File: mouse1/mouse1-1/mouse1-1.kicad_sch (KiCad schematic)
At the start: 30 parts

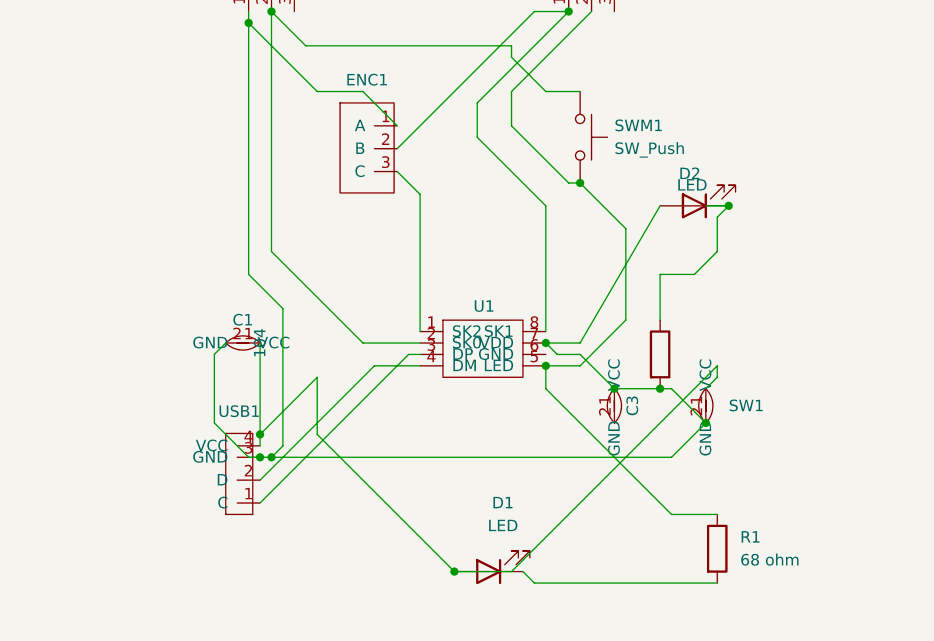
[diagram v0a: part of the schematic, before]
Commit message: Finished PCB - added full labels and all components, even if not actually soldered
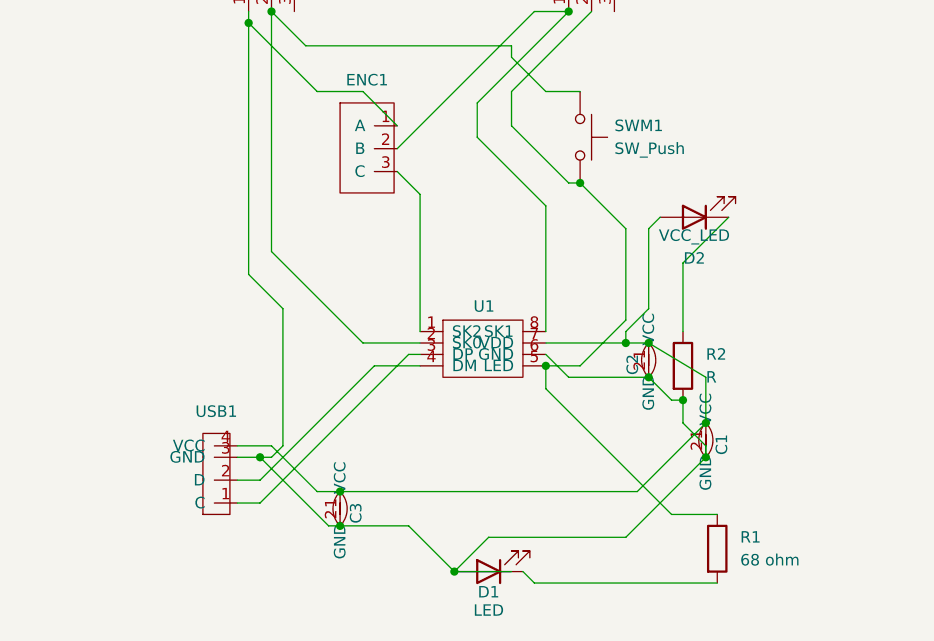
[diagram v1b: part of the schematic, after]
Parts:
- removed D2: LED, LED_THT:LED_D3.0mm_Horizontal_O1.27mm_Z2.0mm, symbol Device:LED
- removed SW1: (no value), IllinoisCapacitor_r3mm_h8mm:IllinoisCapacitor_r3mm_h8mm, symbol SmallCapacitor:SC
- added C2: (no value), SmallCapacitor:SmallCapacitor, symbol SmallCapacitor:SC
- added D2: VCC_LED, LED_THT:LED_D3.0mm_Horizontal_O1.27mm_Z2.0mm, symbol VCC_LED:VCC_LED
- C1: value 104 -> (none); footprint IllinoisCapacitor_r3mm_h8mm:IllinoisCapacitor_r3mm_h8mm -> SmallCapacitor:SmallCapacitor
- C3: footprint IllinoisCapacitor_r3mm_h8mm:IllinoisCapacitor_r3mm_h8mm -> SmallCapacitor:SmallCapacitor; now left out of the parts list
- R2: value 68 ohm -> R; footprint Resistor_THT:R_Axial_DIN0204_L3.6mm_D1.6mm_P5.08mm_Horizontal -> Resistor_THT:R_Axial_DIN0204_L3.6mm_D1.6mm_P5.08mm_Vertical; now left out of the parts list
- SWM1: footprint SW_PUSH_6mm_h7.3mm-2pin:SW_PUSH_6mm_h7.3mm -> 2pin_btn:SW_PUSH_6mm_h7.3mm
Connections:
- net at R2.1: now also D2.1 (A)
- net at C1.2 (VCC), ENC1.1 (A), R2.2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: now also C3.2 (VCC), D1.2 (A), U1.6 (GND), C2.2 (VCC); no longer C3.1 (GND), U1.7 (VDD)
- net at C1.1 (GND), USB1.4 (VCC): now also C3.1 (GND), U1.7 (VDD), C2.1 (GND), D2.2 (K); no longer D1.2 (A)

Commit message: Added schematic to README
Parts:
- ENC1: footprint AlpineRotaryEncoder:AlpineRotaryEncoder -> (none)
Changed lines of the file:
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@@
+	)
+	(symbol
+		(lib_id "AlpineRotaryEncoder:AlpineRotaryEncoderR")
+		(at 87.63 87.63 0)
+		(unit 1)
+		(body_style 1)
+		(exclude_from_sim no)
+		(in_bom yes)
+		(on_board yes)
+		(in_pos_files yes)
+		(dnp no)
+		(fields_autoplaced yes)
+		(property "Reference" "ENC1"
+			(at 90.63 85.09 0)
+			(show_name no)
+			(do_not_autoplace no)
+			(effects
+				(font
+					(size 1.27 1.27)
+				)
+			)
+		)
+		(property "Value" ""
+			(at 87.63 87.63 0)
+			(show_name no)
+			(do_not_autoplace no)
+			(effects
+				(font
+					(size 1.27 1.27)
+				)
+			)
+		)
+		(property "Footprint" ""
+			(at 87.63 87.63 0)
+			(hide yes)
+			(show_name no)
+			(do_not_autoplace no)
+			(effects
+				(font
+					(size 1.27 1.27)
+				)
+			)
+		)
+		(property "Datasheet" ""
+			(at 87.63 87.63 0)
+			(hide yes)
+			(show_name no)
+			(do_not_autoplace no)
+			(effects
+				(font
+					(size 1.27 1.27)
+				)
+			)
+		)
+		(property "Description" ""
+			(at 87.63 87.63 0)
+			(hide yes)
+			(show_name no)
+			(do_not_autoplace no)
+			(effects
+				(font
+					(size 1.27 1.27)
+				)
+			)
+		)
+		(pin "1"
+		)
+		(pin "2"
+		)
+		(pin "3"
+		)
+		(pin "4"
+		)
+		(pin "5"
+		)
+		(instances
+			(project "mouse1-1"
+				(path "/5662a615-6987-4e10-b2bd-1545c5d92725"
+					(reference "ENC1")
+					(unit 1)
+				)
+			)
+		)
 	)
 	(symbol
@@
 					(unit 1)
 				)
-			)
-		)
-	)
-	(symbol
-		(lib_id "AlpineRotaryEncoder:AlpineRotaryEncoderR")
-		(at 87.63 87.63 0)
-		(unit 1)
-		(body_style 1)
-		(exclude_from_sim no)
-		(in_bom yes)
-		(on_board yes)
-		(in_pos_files yes)
-		(dnp no)
-		(fields_autoplaced yes)
-		(property "Reference" "ENC1"
-			(at 90.63 85.09 0)
-			(show_name no)
-			(do_not_autoplace no)
-			(effects
-				(font
-					(size 1.27 1.27)
-				)
-			)
-		)
-		(property "Value" ""
-			(at 87.63 87.63 0)
-			(show_name no)
-			(do_not_autoplace no)
-			(effects
-				(font
-					(size 1.27 1.27)
-				)
-			)
-		)
-		(property "Footprint" "AlpineRotaryEncoder:AlpineRotaryEncoder"
-			(at 87.63 87.63 0)
-			(hide yes)
-			(show_name no)
-			(do_not_autoplace no)
-			(effects
-				(font
-					(size 1.27 1.27)
-				)
-			)
-		)
-		(property "Datasheet" ""
-			(at 87.63 87.63 0)
-			(hide yes)
-			(show_name no)
-			(do_not_autoplace no)
-			(effects
-				(font
-					(size 1.27 1.27)
-				)
-			)
-		)
-		(property "Description" ""
-			(at 87.63 87.63 0)
-			(hide yes)
-			(show_name no)
-			(do_not_autoplace no)
-			(effects
-				(font
-					(size 1.27 1.27)
-				)
-			)
-		)
-		(pin "1"
-		)
-		(pin "3"
-		)
-		(pin "4"
-		)
-		(pin "5"
-		)
-		(pin "2"
-		)
-		(instances
-			(project "mouse1-1"
-				(path "/5662a615-6987-4e10-b2bd-1545c5d92725"
-					(reference "ENC1")
-					(unit 1)
-				)
